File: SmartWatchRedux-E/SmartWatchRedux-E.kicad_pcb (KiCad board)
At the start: 2 copper layers, 21.7 x 64.8 mm, 6 parts, among them CN1 27C256Socket, U1 ROM, U2 DS1315, Y1 32.768 KHz

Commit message: Minor tweakes to board, add -E to name.
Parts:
- C1: footprint Capacitor_SMD:C_0805_2012Metric_Pad1.18x1.45mm_HandSolder -> Capacitor_SMD:C_1206_3216Metric
- moved C1 0.40 mm to (118.1, 67.3)
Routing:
- net VCC: track 39.5 -> 37.8 mm
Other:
- board size 21.7 x 64.8 mm -> 22.2 x 67.3 mm
- board text added: "1"
- board text added: "SMARTWATCH REDUX-E REV 1.0a"
- board text added: "https://github.com/ JayesonLS/SmartWatchRedux"
- board text removed: "SMARTWATCH REDUX REV 1.0a"
- board text removed: "https://github.com/ JayesonLS/TandyCircuitsAndLogic/ tree/master/SmartWatchRedux"

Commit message: SmartWatchRedux-E: Fix version number.
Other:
- board text added: "SMARTWATCH REDUX-E REV 1.1"
- board text removed: "SMARTWATCH REDUX-E REV 1.0a"

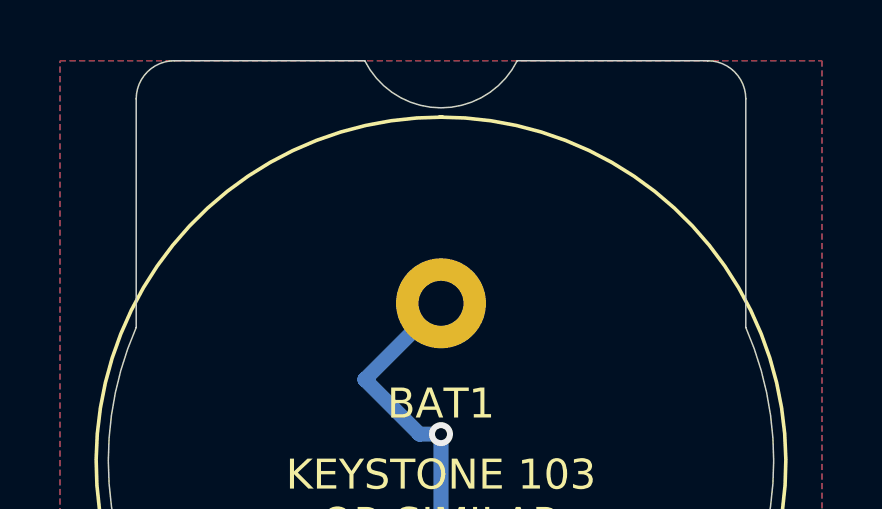
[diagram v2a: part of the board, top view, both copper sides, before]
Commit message: Gerber plots for AssemblyBoard and SmartWatchRedux. Minor board shape change on SmartWatchRedux.
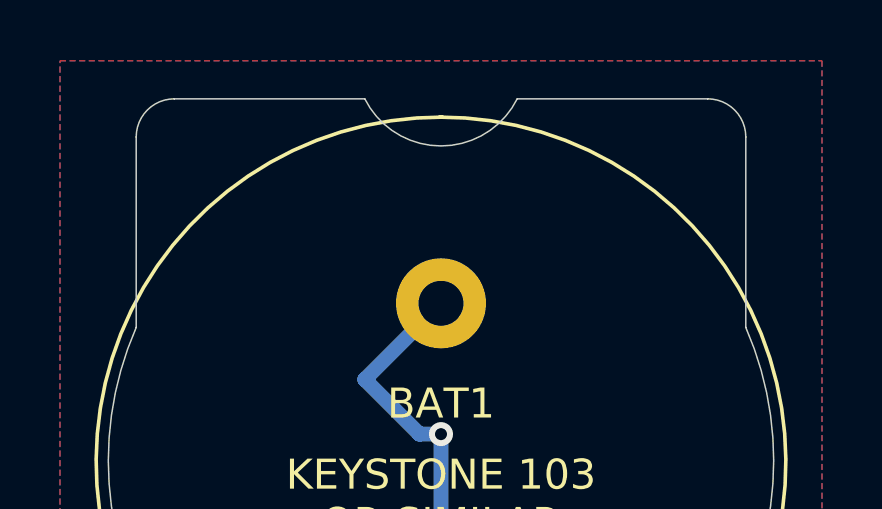
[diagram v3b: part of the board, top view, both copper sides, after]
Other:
- board size 22.2 x 67.3 mm -> 22.2 x 66 mm
